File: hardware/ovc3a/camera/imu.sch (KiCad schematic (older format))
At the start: 2 parts, among them U3 ICM-20948, U4 VN-100

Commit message: ovc3a low-speed expansion board skeleton
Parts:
- removed U3: ICM-20948, Sensor_Motion:InvenSense_QFN-24_3x3mm_P0.4mm, symbol Sensor_motion:ICM-20948
- removed U4: VN-100, IMU:VN-100, symbol IMU:VN-100
- added U3: MPU-9250, Sensor_Motion:InvenSense_QFN-24_3x3mm_P0.4mm, symbol Sensor_motion:MPU-9250
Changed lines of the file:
@@
 $EndDescr
 $Comp
-L IMU:VN-100 U4
-U 1 1 5BFAB777
-P 3000 2850
-F 0 "U4" H 3844 2903 60  0000 L CNN
-F 1 "VN-100" H 3844 2797 60  0000 L CNN
-F 2 "IMU:VN-100" H 3844 2744 60  0001 L CNN
-F 3 "http://www.vectornav.com/docs/default-source/documentation/vn-100-documentation/UM001.pdf?sfvrsn=10" H 3844 2744 60  0001 L CNN
-	1    3000 2850
+L Sensor_motion:MPU-9250 U3
+U 1 1 5C45C0E9
+P 4200 2450
+F 0 "U3" H 4200 1461 50  0000 C CNN
+F 1 "MPU-9250" H 4200 1370 50  0000 C CNN
+F 2 "Sensor_Motion:InvenSense_QFN-24_3x3mm_P0.4mm" H 4200 1450 50  0001 C CNN
+F 3 "https://store.invensense.com/datasheets/invensense/MPU9250REV1.0.pdf" H 4200 2300 50  0001 C CNN
+	1    4200 2450
 	1    0    0    -1
 $EndComp
-$Comp
-L Sensor_motion:ICM-20948 U3
-U 1 1 5C415611
-P 6100 2900
-F 0 "U3" H 6100 1911 50  0000 C CNN
-F 1 "ICM-20948" H 6100 1820 50  0000 C CNN
-F 2 "Sensor_Motion:InvenSense_QFN-24_3x3mm_P0.4mm" H 6100 1900 50  0001 C CNN
-F 3 "http://www.invensense.com/wp-content/uploads/2016/06/DS-000189-ICM-20948-v1.3.pdf" H 6100 2750 50  0001 C CNN
-	1    6100 2900
-	1    0    0    -1
-$EndComp

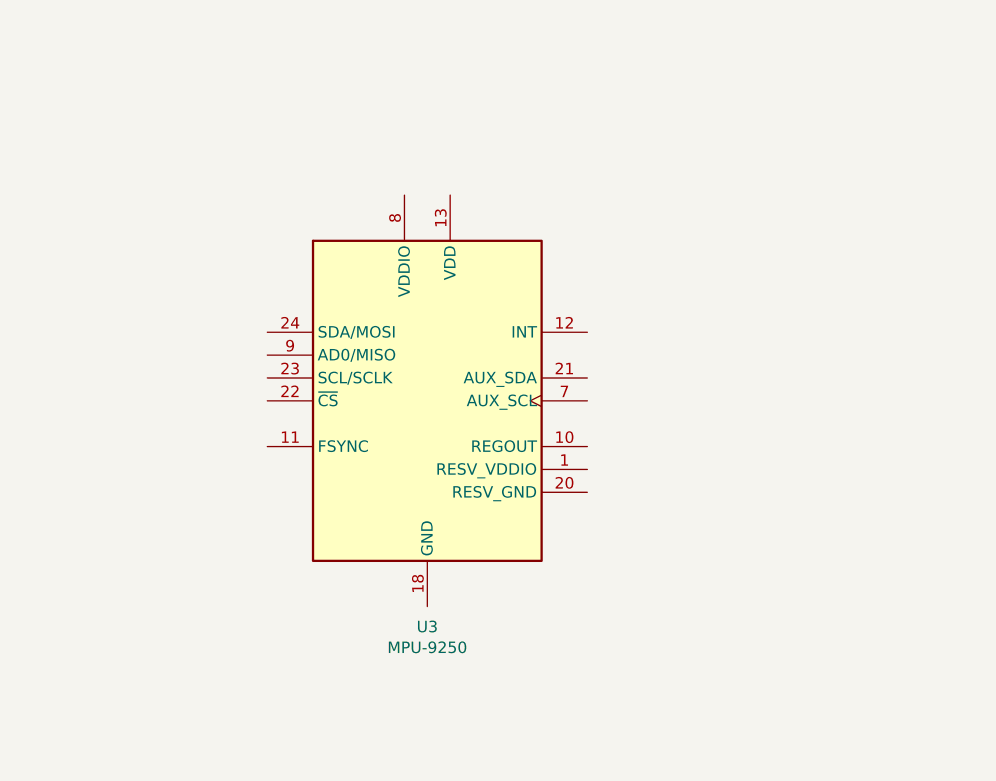
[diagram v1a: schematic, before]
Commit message: Preliminary component placement
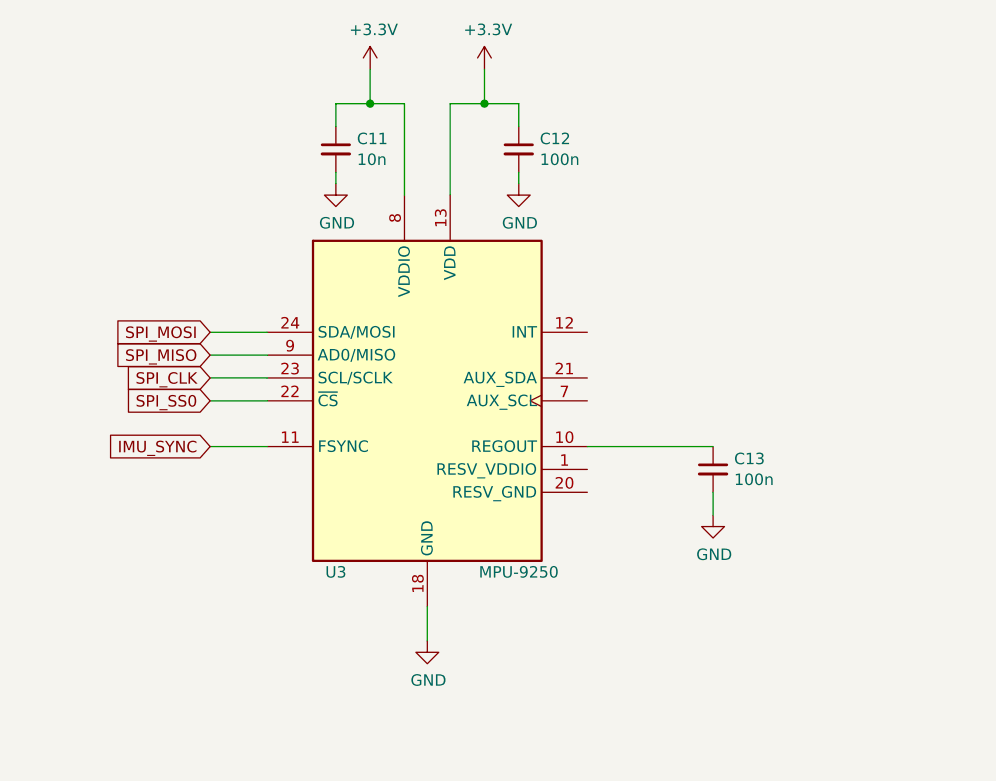
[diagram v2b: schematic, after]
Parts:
- added C11: 10n, Capacitor_SMD:C_0402_1005Metric, symbol Device:C_Small
- added C12, C13: 100n, Capacitor_SMD:C_0402_1005Metric, symbol Device:C_Small
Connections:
- net at U3.10 (REGOUT): now also C13.1
- net IMU_SYNC: now reaches U3.11 (FSYNC)
- net +3V3: now reaches U3.13 (VDD)
- net +3V3: now also U3.8 (VDDIO), C11.1, C12.1
- net GND: now reaches U3.18 (GND)
- net GND: now also C11.2, C12.2, C13.2
- net SPI_SS0: now reaches U3.22 (~CS)
- net SPI_CLK: now reaches U3.23 (SCL/SCLK)
- net SPI_MOSI: now reaches U3.24 (SDA/MOSI)
- net SPI_MISO: now reaches U3.9 (AD0/MISO)
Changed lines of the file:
@@
 U 1 1 5C45C0E9
 P 4200 2450
-F 0 "U3" H 4200 1461 50  0000 C CNN
-F 1 "MPU-9250" H 4200 1370 50  0000 C CNN
+F 0 "U3" H 3800 1700 50  0000 C CNN
+F 1 "MPU-9250" H 4600 1700 50  0000 C CNN
 F 2 "Sensor_Motion:InvenSense_QFN-24_3x3mm_P0.4mm" H 4200 1450 50  0001 C CNN
 F 3 "https://store.invensense.com/datasheets/invensense/MPU9250REV1.0.pdf" H 4200 2300 50  0001 C CNN
@@
 	1    0    0    -1
 $EndComp
+Text GLabel 3250 2450 0    50   Input ~ 0
+SPI_SS0
+Wire Wire Line
+	3250 2450 3500 2450
+Text GLabel 3250 2350 0    50   Input ~ 0
+SPI_CLK
+Wire Wire Line
+	3250 2350 3500 2350
+Text GLabel 3250 2150 0    50   Input ~ 0
+SPI_MOSI
+Wire Wire Line
+	3250 2150 3500 2150
+Text GLabel 3250 2250 0    50   Input ~ 0
+SPI_MISO
+Wire Wire Line
+	3250 2250 3500 2250
+$Comp
+L power:GND #PWR0132
+U 1 1 5C51509B
+P 4200 3500
+F 0 "#PWR0132" H 4200 3250 50  0001 C CNN
+F 1 "GND" H 4205 3327 50  0000 C CNN
+F 2 "" H 4200 3500 50  0001 C CNN
+F 3 "" H 4200 3500 50  0001 C CNN
+	1    4200 3500
+	1    0    0    -1
+$EndComp
+Wire Wire Line
+	4200 3500 4200 3350
+$Comp
+L power:+3.3V #PWR0133
+U 1 1 5C5162B0
+P 4450 1000
+F 0 "#PWR0133" H 4450 850 50  0001 C CNN
+F 1 "+3.3V" H 4465 1173 50  0000 C CNN
+F 2 "" H 4450 1000 50  0001 C CNN
+F 3 "" H 4450 1000 50  0001 C CNN
+	1    4450 1000
+	1    0    0    -1
+$EndComp
+Wire Wire Line
+	4450 1150 4450 1000
+$Comp
+L Device:C_Small C12
+U 1 1 5C517195
+P 4600 1350
+F 0 "C12" H 4692 1396 50  0000 L CNN
+F 1 "100n" H 4692 1305 50  0000 L CNN
+F 2 "Capacitor_SMD:C_0402_1005Metric" H 4600 1350 50  0001 C CNN
+F 3 "~" H 4600 1350 50  0001 C CNN
+	1    4600 1350
+	1    0    0    -1
+$EndComp
+$Comp
+L Device:C_Small C11
+U 1 1 5C517369
+P 3800 1350
+F 0 "C11" H 3892 1396 50  0000 L CNN
+F 1 "10n" H 3892 1305 50  0000 L CNN
+F 2 "Capacitor_SMD:C_0402_1005Metric" H 3800 1350 50  0001 C CNN
+F 3 "~" H 3800 1350 50  0001 C CNN
+	1    3800 1350
+	1    0    0    -1
+$EndComp
+Wire Wire Line
+	4100 1150 3950 1150
+Wire Wire Line
+	3800 1150 3800 1250
+Wire Wire Line
+	4300 1150 4450 1150
+Wire Wire Line
+	4600 1150 4600 1250
+Connection ~ 4450 1150
+Wire Wire Line
+	4450 1150 4600 1150
+$Comp
+L power:+3.3V #PWR0134
+U 1 1 5C51A324
+P 3950 1000
+F 0 "#PWR0134" H 3950 850 50  0001 C CNN
+F 1 "+3.3V" H 3965 1173 50  0000 C CNN
+F 2 "" H 3950 1000 50  0001 C CNN
+F 3 "" H 3950 1000 50  0001 C CNN
+	1    3950 1000
+	1    0    0    -1
+$EndComp
+Wire Wire Line
+	3950 1000 3950 1150
+Connection ~ 3950 1150
+Wire Wire Line
+	3950 1150 3800 1150
+$Comp
+L power:GND #PWR0135
+U 1 1 5C51A701
+P 3800 1500
+F 0 "#PWR0135" H 3800 1250 50  0001 C CNN
+F 1 "GND" H 3805 1327 50  0000 C CNN
+F 2 "" H 3800 1500 50  0001 C CNN
+F 3 "" H 3800 1500 50  0001 C CNN
+	1    3800 1500
+	1    0    0    -1
+$EndComp
+Wire Wire Line
+	3800 1500 3800 1450
+Wire Wire Line
+	4100 1150 4100 1550
+Wire Wire Line
+	4300 1150 4300 1550
+$Comp
+L power:GND #PWR0136
+U 1 1 5C51BB0B
+P 4600 1500
+F 0 "#PWR0136" H 4600 1250 50  0001 C CNN
+F 1 "GND" H 4605 1327 50  0000 C CNN
+F 2 "" H 4600 1500 50  0001 C CNN
+F 3 "" H 4600 1500 50  0001 C CNN
+	1    4600 1500
+	1    0    0    -1
+$EndComp
+Wire Wire Line
+	4600 1500 4600 1450
+$Comp
+L Device:C_Small C13
+U 1 1 5C51C8A5
+P 5450 2750
+F 0 "C13" H 5542 2796 50  0000 L CNN
+F 1 "100n" H 5542 2705 50  0000 L CNN
+F 2 "Capacitor_SMD:C_0402_1005Metric" H 5450 2750 50  0001 C CNN
+F 3 "~" H 5450 2750 50  0001 C CNN
+	1    5450 2750
+	1    0    0    -1
+$EndComp
+Wire Wire Line
+	4900 2650 5450 2650
+$Comp
+L power:GND #PWR0137
+U 1 1 5C51D27C
+P 5450 2950
+F 0 "#PWR0137" H 5450 2700 50  0001 C CNN
+F 1 "GND" H 5455 2777 50  0000 C CNN
+F 2 "" H 5450 2950 50  0001 C CNN
+F 3 "" H 5450 2950 50  0001 C CNN
+	1    5450 2950
+	1    0    0    -1
+$EndComp
+Wire Wire Line
+	5450 2950 5450 2850
+Wire Wire Line
+	3250 2650 3500 2650
+Text GLabel 3250 2650 0    50   Input ~ 0
+IMU_SYNC
 $EndSCHEMATC

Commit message: Placement completed, pre FPGA IO assignment
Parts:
- C11: value 10n -> 100n
- U3: value MPU-9250 -> ICM-20948; symbol Sensor_motion:MPU-9250 -> Sensor_motion:ICM-20948
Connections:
- net +3V3: no longer C11.1, U3.8 (VDDIO)
- net GND: now also U3.20 (GND)
- net ICM-IMU_INT1: now reaches U3.12 (INT1)
- net IMU_SYNC renamed ICM-IMU_SYNC
- net SPI_CLK renamed ICM-SPI_CLK
- net SPI_MISO renamed ICM-SPI_MOSI
- net SPI_MOSI renamed ICM-SPI_MISO
- net SPI_SS0 renamed ICM-SPI_CS
- new net +1V8: C11.1, U3.8 (VDDIO)
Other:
- moved on the sheet: C13
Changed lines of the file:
@@
 $EndDescr
 $Comp
-L Sensor_motion:MPU-9250 U3
+L Sensor_motion:ICM-20948 U3
 U 1 1 5C45C0E9
 P 4200 2450
-F 0 "U3" H 3800 1700 50  0000 C CNN
-F 1 "MPU-9250" H 4600 1700 50  0000 C CNN
+F 0 "U3" H 3800 1800 50  0000 C CNN
+F 1 "ICM-20948" H 4600 1800 50  0000 C CNN
 F 2 "Sensor_Motion:InvenSense_QFN-24_3x3mm_P0.4mm" H 4200 1450 50  0001 C CNN
 F 3 "https://store.invensense.com/datasheets/invensense/MPU9250REV1.0.pdf" H 4200 2300 50  0001 C CNN
@@
 	1    0    0    -1
 $EndComp
-Text GLabel 3250 2450 0    50   Input ~ 0
-SPI_SS0
+Text GLabel 3450 2450 0    50   Input ~ 0
+ICM-SPI_CS
 Wire Wire Line
-	3250 2450 3500 2450
-Text GLabel 3250 2350 0    50   Input ~ 0
-SPI_CLK
+	3450 2450 3700 2450
+Text GLabel 3450 2350 0    50   Input ~ 0
+ICM-SPI_CLK
 Wire Wire Line
-	3250 2350 3500 2350
-Text GLabel 3250 2150 0    50   Input ~ 0
-SPI_MOSI
+	3450 2350 3700 2350
+Text GLabel 3450 2150 0    50   Input ~ 0
+ICM-SPI_MOSI
 Wire Wire Line
-	3250 2150 3500 2150
-Text GLabel 3250 2250 0    50   Input ~ 0
-SPI_MISO
+	3450 2150 3700 2150
+Text GLabel 3450 2250 0    50   Input ~ 0
+ICM-SPI_MISO
 Wire Wire Line
-	3250 2250 3500 2250
+	3450 2250 3700 2250
 $Comp
 L power:GND #PWR0132
 U 1 1 5C51509B
-P 4200 3500
-F 0 "#PWR0132" H 4200 3250 50  0001 C CNN
-F 1 "GND" H 4205 3327 50  0000 C CNN
-F 2 "" H 4200 3500 50  0001 C CNN
-F 3 "" H 4200 3500 50  0001 C CNN
-	1    4200 3500
+P 4200 3300
+F 0 "#PWR0132" H 4200 3050 50  0001 C CNN
+F 1 "GND" H 4205 3127 50  0000 C CNN
+F 2 "" H 4200 3300 50  0001 C CNN
+F 3 "" H 4200 3300 50  0001 C CNN
+	1    4200 3300
 	1    0    0    -1
 $EndComp
 Wire Wire Line
-	4200 3500 4200 3350
+	4200 3300 4200 3150
 $Comp
 L power:+3.3V #PWR0133
@@
 P 3800 1350
 F 0 "C11" H 3892 1396 50  0000 L CNN
-F 1 "10n" H 3892 1305 50  0000 L CNN
+F 1 "100n" H 3892 1305 50  0000 L CNN
 F 2 "Capacitor_SMD:C_0402_1005Metric" H 3800 1350 50  0001 C CNN
 F 3 "~" H 3800 1350 50  0001 C CNN
@@
 Wire Wire Line
 	4450 1150 4600 1150
-$Comp
-L power:+3.3V #PWR0134
-U 1 1 5C51A324
-P 3950 1000
-F 0 "#PWR0134" H 3950 850 50  0001 C CNN
-F 1 "+3.3V" H 3965 1173 50  0000 C CNN
-F 2 "" H 3950 1000 50  0001 C CNN
-F 3 "" H 3950 1000 50  0001 C CNN
-	1    3950 1000
-	1    0    0    -1
-$EndComp
 Wire Wire Line
 	3950 1000 3950 1150
@@
 Wire Wire Line
 	3800 1500 3800 1450
-Wire Wire Line
-	4100 1150 4100 1550
-Wire Wire Line
-	4300 1150 4300 1550
 $Comp
 L power:GND #PWR0136
@@
 L Device:C_Small C13
 U 1 1 5C51C8A5
-P 5450 2750
-F 0 "C13" H 5542 2796 50  0000 L CNN
-F 1 "100n" H 5542 2705 50  0000 L CNN
-F 2 "Capacitor_SMD:C_0402_1005Metric" H 5450 2750 50  0001 C CNN
-F 3 "~" H 5450 2750 50  0001 C CNN
-	1    5450 2750
+P 5250 2750
+F 0 "C13" H 5342 2796 50  0000 L CNN
+F 1 "100n" H 5342 2705 50  0000 L CNN
+F 2 "Capacitor_SMD:C_0402_1005Metric" H 5250 2750 50  0001 C CNN
+F 3 "~" H 5250 2750 50  0001 C CNN
+	1    5250 2750
 	1    0    0    -1
 $EndComp
 Wire Wire Line
-	4900 2650 5450 2650
+	4700 2650 5250 2650
 $Comp
 L power:GND #PWR0137
 U 1 1 5C51D27C
-P 5450 2950
-F 0 "#PWR0137" H 5450 2700 50  0001 C CNN
-F 1 "GND" H 5455 2777 50  0000 C CNN
-F 2 "" H 5450 2950 50  0001 C CNN
-F 3 "" H 5450 2950 50  0001 C CNN
-	1    5450 2950
+P 5250 2950
+F 0 "#PWR0137" H 5250 2700 50  0001 C CNN
+F 1 "GND" H 5255 2777 50  0000 C CNN
+F 2 "" H 5250 2950 50  0001 C CNN
+F 3 "" H 5250 2950 50  0001 C CNN
+	1    5250 2950
 	1    0    0    -1
 $EndComp
 Wire Wire Line
-	5450 2950 5450 2850
+	5250 2950 5250 2850
 Wire Wire Line
-	3250 2650 3500 2650
-Text GLabel 3250 2650 0    50   Input ~ 0
-IMU_SYNC
+	3450 2650 3700 2650
+Text GLabel 3450 2650 0    50   Input ~ 0
+ICM-IMU_SYNC
+Wire Wire Line
+	4100 1150 4100 1750
+Wire Wire Line
+	4300 1150 4300 1750
+Wire Wire Line
+	3450 2750 3700 2750
+Text GLabel 3450 2750 0    50   Input ~ 0
+ICM-IMU_INT1
+$Comp
+L power:+1V8 #PWR?
+U 1 1 5C55489B
+P 3950 1000
+F 0 "#PWR?" H 3950 850 50  0001 C CNN
+F 1 "+1V8" H 3965 1173 50  0000 C CNN
+F 2 "" H 3950 1000 50  0001 C CNN
+F 3 "" H 3950 1000 50  0001 C CNN
+	1    3950 1000
+	1    0    0    -1
+$EndComp
 $EndSCHEMATC

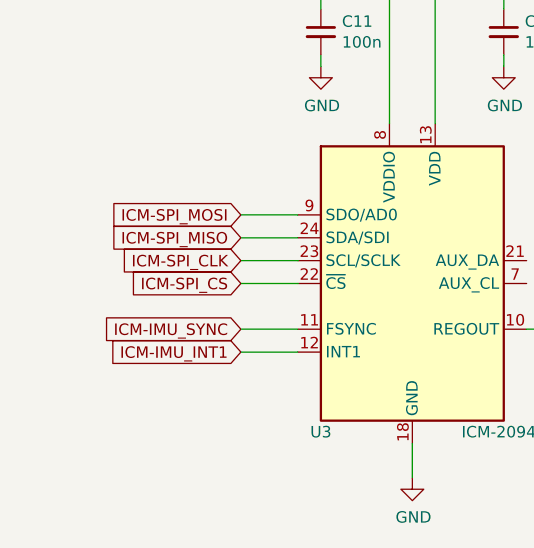
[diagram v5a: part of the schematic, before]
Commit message: Preliminary placement of MIPI lanes, finished routing first imager
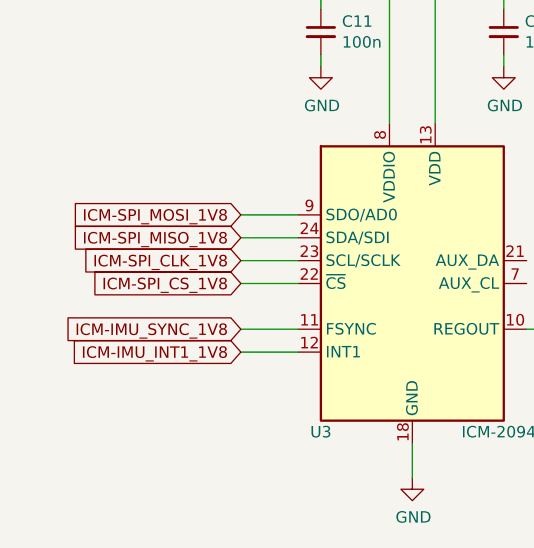
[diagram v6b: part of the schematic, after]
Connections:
- net ICM-IMU_INT1 renamed ICM-IMU_INT1_1V8
- net ICM-IMU_SYNC renamed ICM-IMU_SYNC_1V8
- net ICM-SPI_CLK renamed ICM-SPI_CLK_1V8
- net ICM-SPI_CS renamed ICM-SPI_CS_1V8
- net ICM-SPI_MISO renamed ICM-SPI_MISO_1V8
- net ICM-SPI_MOSI renamed ICM-SPI_MOSI_1V8
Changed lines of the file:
@@
 $EndComp
 Text GLabel 3450 2450 0    50   Input ~ 0
-ICM-SPI_CS
+ICM-SPI_CS_1V8
 Wire Wire Line
 	3450 2450 3700 2450
 Text GLabel 3450 2350 0    50   Input ~ 0
-ICM-SPI_CLK
+ICM-SPI_CLK_1V8
 Wire Wire Line
 	3450 2350 3700 2350
 Text GLabel 3450 2150 0    50   Input ~ 0
-ICM-SPI_MOSI
+ICM-SPI_MOSI_1V8
 Wire Wire Line
 	3450 2150 3700 2150
 Text GLabel 3450 2250 0    50   Input ~ 0
-ICM-SPI_MISO
+ICM-SPI_MISO_1V8
 Wire Wire Line
 	3450 2250 3700 2250
@@
 	3450 2650 3700 2650
 Text GLabel 3450 2650 0    50   Input ~ 0
-ICM-IMU_SYNC
+ICM-IMU_SYNC_1V8
 Wire Wire Line
 	4100 1150 4100 1750
@@
 	3450 2750 3700 2750
 Text GLabel 3450 2750 0    50   Input ~ 0
-ICM-IMU_INT1
+ICM-IMU_INT1_1V8
 $Comp
 L power:+1V8 #PWR0134

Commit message: place/route progress
 * rotate imagers 180 degrees
 * re-route east imager
 * assign east 1v2-1v8 outbound shifter signals
 * move IMU chip to east side of board
 * power plane cleanup on east side
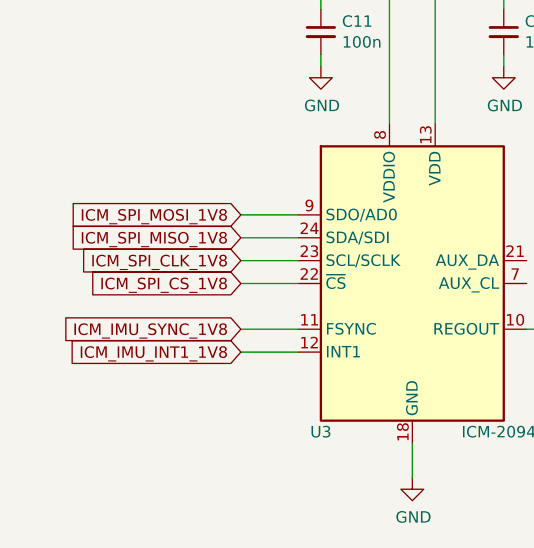
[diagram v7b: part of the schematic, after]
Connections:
- net ICM-IMU_INT1_1V8 renamed ICM_IMU_INT1_1V8
- net ICM-IMU_SYNC_1V8 renamed ICM_IMU_SYNC_1V8
- net ICM-SPI_CLK_1V8 renamed ICM_SPI_CLK_1V8
- net ICM-SPI_CS_1V8 renamed ICM_SPI_CS_1V8
- net ICM-SPI_MISO_1V8 renamed ICM_SPI_MISO_1V8
- net ICM-SPI_MOSI_1V8 renamed ICM_SPI_MOSI_1V8
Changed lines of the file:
@@
 $EndComp
 Text GLabel 3450 2450 0    50   Input ~ 0
-ICM-SPI_CS_1V8
+ICM_SPI_CS_1V8
 Wire Wire Line
 	3450 2450 3700 2450
 Text GLabel 3450 2350 0    50   Input ~ 0
-ICM-SPI_CLK_1V8
+ICM_SPI_CLK_1V8
 Wire Wire Line
 	3450 2350 3700 2350
 Text GLabel 3450 2150 0    50   Input ~ 0
-ICM-SPI_MOSI_1V8
+ICM_SPI_MOSI_1V8
 Wire Wire Line
 	3450 2150 3700 2150
 Text GLabel 3450 2250 0    50   Input ~ 0
-ICM-SPI_MISO_1V8
+ICM_SPI_MISO_1V8
 Wire Wire Line
 	3450 2250 3700 2250
@@
 	3450 2650 3700 2650
 Text GLabel 3450 2650 0    50   Input ~ 0
-ICM-IMU_SYNC_1V8
+ICM_IMU_SYNC_1V8
 Wire Wire Line
 	4100 1150 4100 1750
@@
 	3450 2750 3700 2750
 Text GLabel 3450 2750 0    50   Input ~ 0
-ICM-IMU_INT1_1V8
+ICM_IMU_INT1_1V8
 $Comp
 L power:+1V8 #PWR0134

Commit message: Finished routing, start adding parts to BOM
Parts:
- C11, C12, C13: D1N (none) -> Digikey; D1PN (none) -> 1276-1004-1-ND; MFN (none) -> Samsung Electro-Mechanics; MPN (none) -> CL05F104ZO5NNNC
- U3: D1N (none) -> Digikey; D1PN (none) -> 1428-1123-1-ND; MFN (none) -> TDK InvenSense; MPN (none) -> ICM-20948
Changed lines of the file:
@@
 F 2 "Sensor_Motion:InvenSense_QFN-24_3x3mm_P0.4mm" H 4200 1450 50  0001 C CNN
 F 3 "https://store.invensense.com/datasheets/invensense/MPU9250REV1.0.pdf" H 4200 2300 50  0001 C CNN
+F 4 "Digikey" H 3800 1900 50  0001 C CNN "D1N"
+F 5 "1428-1123-1-ND" H 3800 1900 50  0001 C CNN "D1PN"
+F 6 "TDK InvenSense" H 3800 1900 50  0001 C CNN "MFN"
+F 7 "ICM-20948" H 3800 1900 50  0001 C CNN "MPN"
 	1    4200 2450
 	1    0    0    -1
 $EndComp
-Text GLabel 3450 2450 0    50   Input ~ 0
-ICM_SPI_CS_1V8
-Wire Wire Line
-	3450 2450 3700 2450
-Text GLabel 3450 2350 0    50   Input ~ 0
-ICM_SPI_CLK_1V8
-Wire Wire Line
-	3450 2350 3700 2350
-Text GLabel 3450 2150 0    50   Input ~ 0
-ICM_SPI_MOSI_1V8
-Wire Wire Line
-	3450 2150 3700 2150
-Text GLabel 3450 2250 0    50   Input ~ 0
-ICM_SPI_MISO_1V8
-Wire Wire Line
-	3450 2250 3700 2250
 $Comp
 L power:GND #PWR0132
@@
 	1    0    0    -1
 $EndComp
-Wire Wire Line
-	4200 3300 4200 3150
 $Comp
 L power:+3.3V #PWR0133
@@
 	1    0    0    -1
 $EndComp
-Wire Wire Line
-	4450 1150 4450 1000
 $Comp
 L Device:C_Small C12
@@
 F 2 "Capacitor_SMD:C_0402_1005Metric" H 4600 1350 50  0001 C CNN
 F 3 "~" H 4600 1350 50  0001 C CNN
+F 4 "Digikey" H 4692 1496 50  0001 C CNN "D1N"
+F 5 "1276-1004-1-ND" H 4692 1496 50  0001 C CNN "D1PN"
+F 6 "Samsung Electro-Mechanics" H 4692 1496 50  0001 C CNN "MFN"
+F 7 "CL05F104ZO5NNNC" H 4692 1496 50  0001 C CNN "MPN"
 	1    4600 1350
 	1    0    0    -1
@@
 F 2 "Capacitor_SMD:C_0402_1005Metric" H 3800 1350 50  0001 C CNN
 F 3 "~" H 3800 1350 50  0001 C CNN
+F 4 "Digikey" H 3892 1496 50  0001 C CNN "D1N"
+F 5 "1276-1004-1-ND" H 3892 1496 50  0001 C CNN "D1PN"
+F 6 "Samsung Electro-Mechanics" H 3892 1496 50  0001 C CNN "MFN"
+F 7 "CL05F104ZO5NNNC" H 3892 1496 50  0001 C CNN "MPN"
 	1    3800 1350
 	1    0    0    -1
 $EndComp
-Wire Wire Line
-	4100 1150 3950 1150
-Wire Wire Line
-	3800 1150 3800 1250
-Wire Wire Line
-	4300 1150 4450 1150
-Wire Wire Line
-	4600 1150 4600 1250
-Connection ~ 4450 1150
-Wire Wire Line
-	4450 1150 4600 1150
-Wire Wire Line
-	3950 1000 3950 1150
-Connection ~ 3950 1150
-Wire Wire Line
-	3950 1150 3800 1150
 $Comp
 L power:GND #PWR0135
@@
 	1    0    0    -1
 $EndComp
-Wire Wire Line
-	3800 1500 3800 1450
 $Comp
 L power:GND #PWR0136
@@
 	1    0    0    -1
 $EndComp
-Wire Wire Line
-	4600 1500 4600 1450
 $Comp
 L Device:C_Small C13
@@
 F 2 "Capacitor_SMD:C_0402_1005Metric" H 5250 2750 50  0001 C CNN
 F 3 "~" H 5250 2750 50  0001 C CNN
+F 4 "Digikey" H 5342 2896 50  0001 C CNN "D1N"
+F 5 "1276-1004-1-ND" H 5342 2896 50  0001 C CNN "D1PN"
+F 6 "Samsung Electro-Mechanics" H 5342 2896 50  0001 C CNN "MFN"
+F 7 "CL05F104ZO5NNNC" H 5342 2896 50  0001 C CNN "MPN"
 	1    5250 2750
 	1    0    0    -1
 $EndComp
-Wire Wire Line
-	4700 2650 5250 2650
 $Comp
 L power:GND #PWR0137
@@
 	1    0    0    -1
 $EndComp
-Wire Wire Line
-	5250 2950 5250 2850
-Wire Wire Line
-	3450 2650 3700 2650
-Text GLabel 3450 2650 0    50   Input ~ 0
-ICM_IMU_SYNC_1V8
-Wire Wire Line
-	4100 1150 4100 1750
-Wire Wire Line
-	4300 1150 4300 1750
-Wire Wire Line
-	3450 2750 3700 2750
-Text GLabel 3450 2750 0    50   Input ~ 0
-ICM_IMU_INT1_1V8
 $Comp
 L power:+1V8 #PWR0134
@@
 	1    0    0    -1
 $EndComp
+Text GLabel 3450 2450 0    50   Input ~ 0
+ICM_SPI_CS_1V8
+Text GLabel 3450 2350 0    50   Input ~ 0
+ICM_SPI_CLK_1V8
+Text GLabel 3450 2150 0    50   Input ~ 0
+ICM_SPI_MOSI_1V8
+Text GLabel 3450 2250 0    50   Input ~ 0
+ICM_SPI_MISO_1V8
+Text GLabel 3450 2650 0    50   Input ~ 0
+ICM_IMU_SYNC_1V8
+Text GLabel 3450 2750 0    50   Input ~ 0
+ICM_IMU_INT1_1V8
+Wire Wire Line
+	3450 2450 3700 2450
+Wire Wire Line
+	3450 2350 3700 2350
+Wire Wire Line
+	3450 2150 3700 2150
+Wire Wire Line
+	3450 2250 3700 2250
+Wire Wire Line
+	4200 3300 4200 3150
+Wire Wire Line
+	4450 1150 4450 1000
+Wire Wire Line
+	4100 1150 3950 1150
+Wire Wire Line
+	3800 1150 3800 1250
+Wire Wire Line
+	4300 1150 4450 1150
+Wire Wire Line
+	4600 1150 4600 1250
+Wire Wire Line
+	4450 1150 4600 1150
+Wire Wire Line
+	3950 1000 3950 1150
+Wire Wire Line
+	3950 1150 3800 1150
+Wire Wire Line
+	3800 1500 3800 1450
+Wire Wire Line
+	4600 1500 4600 1450
+Wire Wire Line
+	4700 2650 5250 2650
+Wire Wire Line
+	5250 2950 5250 2850
+Wire Wire Line
+	3450 2650 3700 2650
+Wire Wire Line
+	4100 1150 4100 1750
+Wire Wire Line
+	4300 1150 4300 1750
+Wire Wire Line
+	3450 2750 3700 2750
+Connection ~ 4450 1150
+Connection ~ 3950 1150
 $EndSCHEMATC
